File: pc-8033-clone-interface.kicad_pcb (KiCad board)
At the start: 2 copper layers, 95.2 x 67.3 mm, 19 parts, among them J2 80s31, U2 74LS32, U3 74LS04, U4 82C55A, U5 74LS30

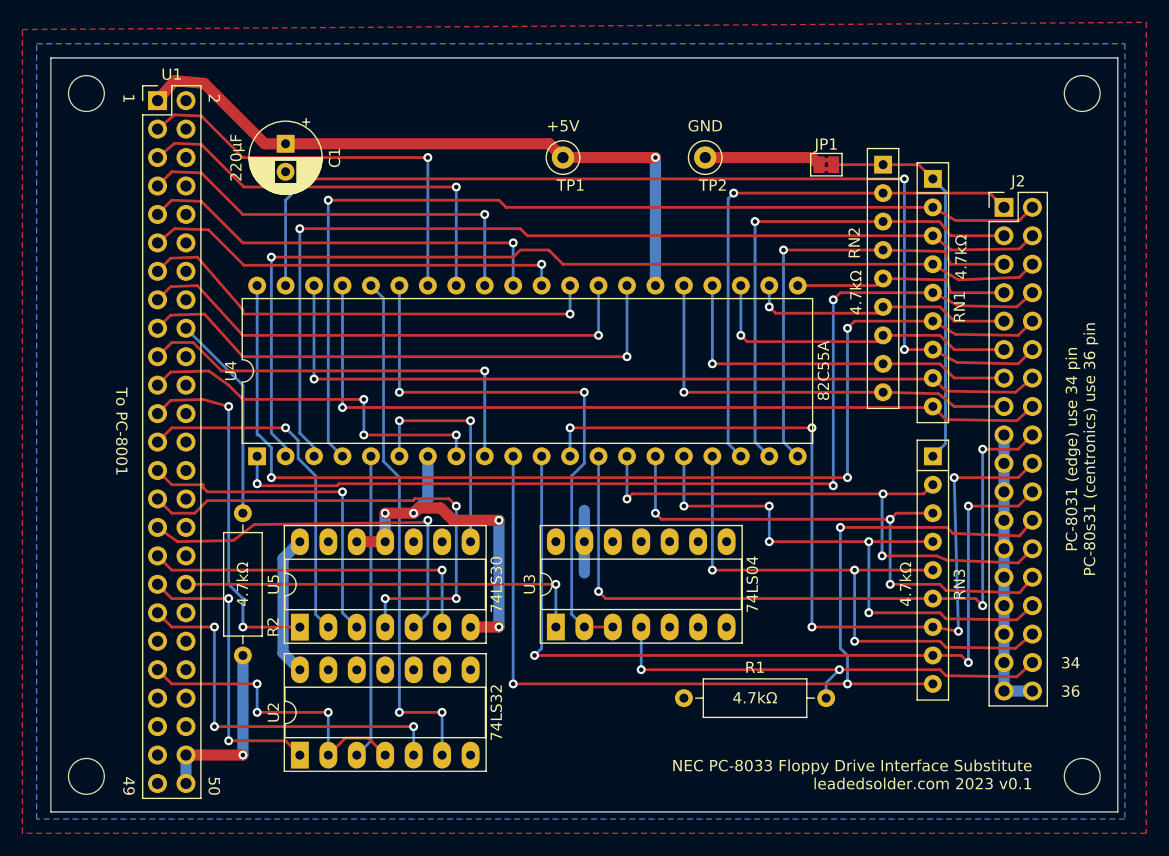
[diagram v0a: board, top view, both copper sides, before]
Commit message: Rotate 50-pin connector
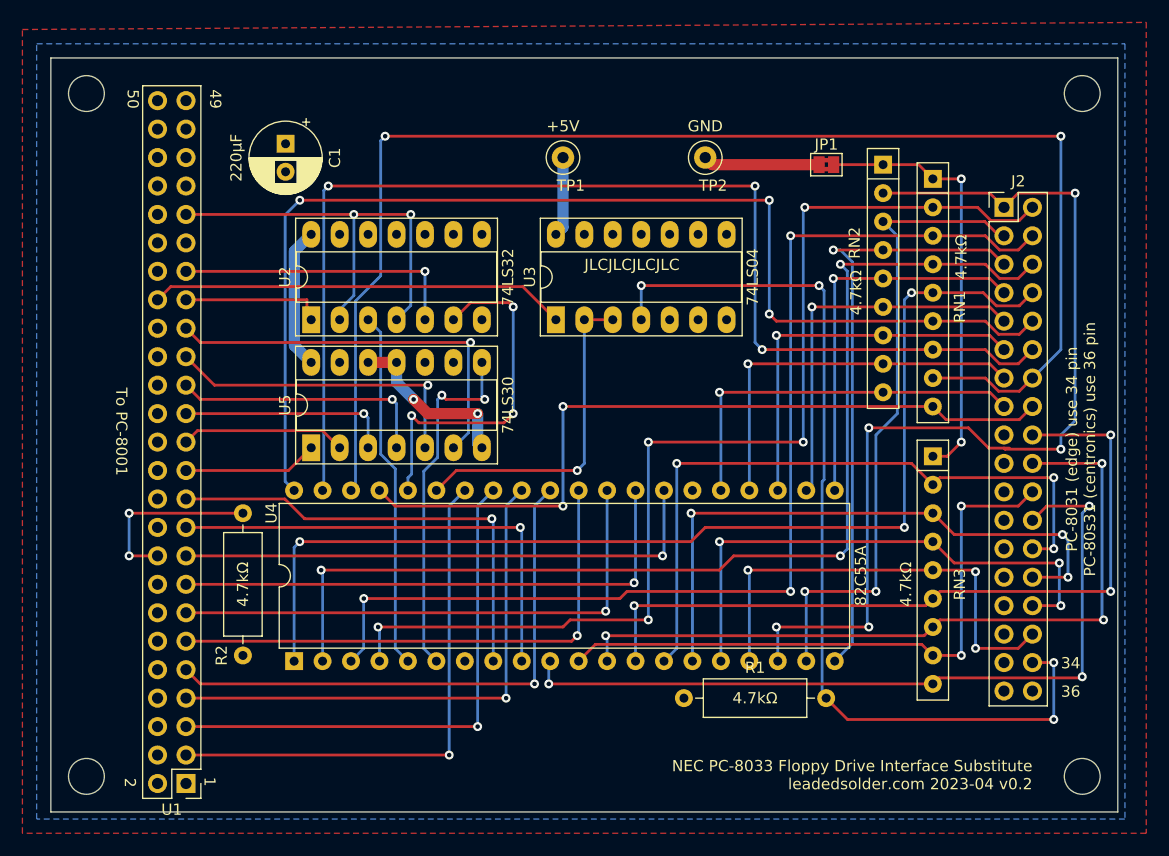
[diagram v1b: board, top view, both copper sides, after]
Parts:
- moved U1 61.0 mm to (116.8, 135.9), turned to 180 degrees
- moved U2 38.9 mm to (128.0, 94.5)
- moved U3 27.4 mm to (149.9, 94.5)
- moved U4 18.6 mm to (126.5, 125.0)
- moved U5 16.0 mm to (128.0, 105.9)
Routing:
- net GND: track 91.5 -> 26.3 mm, vias 5 -> 2
- net +5V: track 72.1 -> 19.8 mm, vias 1 -> 0
- net /pa6: track 73.5 -> 125.7 mm, vias 1 -> 2
- net Net-(J2-Pin_34): track 42.5 -> 84.3 mm, vias 2 -> 4
- net /pb0: track 48.8 -> 89.3 mm, vias 1 -> 5
- net /pc6: track 77.3 -> 55.4 mm, vias 3 -> 2
- net Net-(U1-AB5): track 45.2 -> 23.4 mm, vias 3 -> 1
- net /RESET: track 50.5 -> 29.6 mm, vias 2 -> 1
- net Net-(U1-AB2): track 32.2 -> 12.0 mm, vias 2 -> 0
- net /pc7: track 90.1 -> 71.1 mm
- net Net-(U1-AB3): track 31.3 -> 14.8 mm, vias 1 -> 0
- net /pb3: track 19.6 -> 34.7 mm, vias 0 -> 1
- net /pb2: track 39.3 -> 54.2 mm
- net /~{8255_WR}: track 46.8 -> 32.1 mm, vias 2 -> 3
- net /pa5: track 91.1 -> 105.5 mm
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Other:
- board text added: "JLCJLCJLCJLC"
- board text added: "NEC PC-8033 Floppy Drive Interface Substitute leadedsolder.com 2023-04 v0.2"
- board text removed: "NEC PC-8033 Floppy Drive Interface Substitute leadedsolder.com 2023 v0.1"

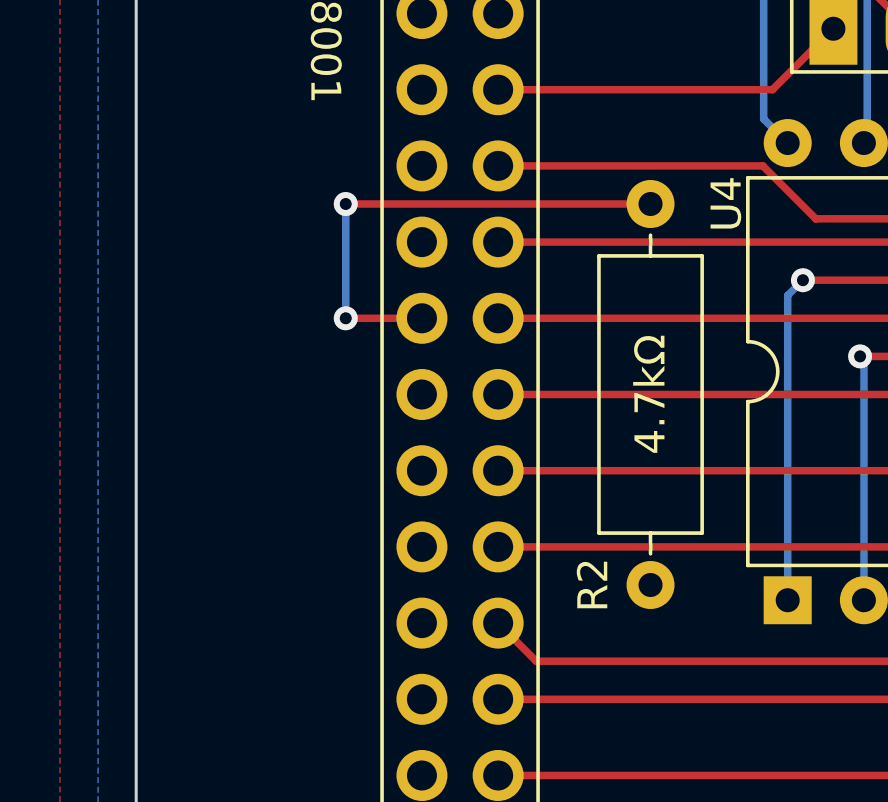
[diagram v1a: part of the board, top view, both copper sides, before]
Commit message: Short the EXTON pin instead of trying to gently pull it down
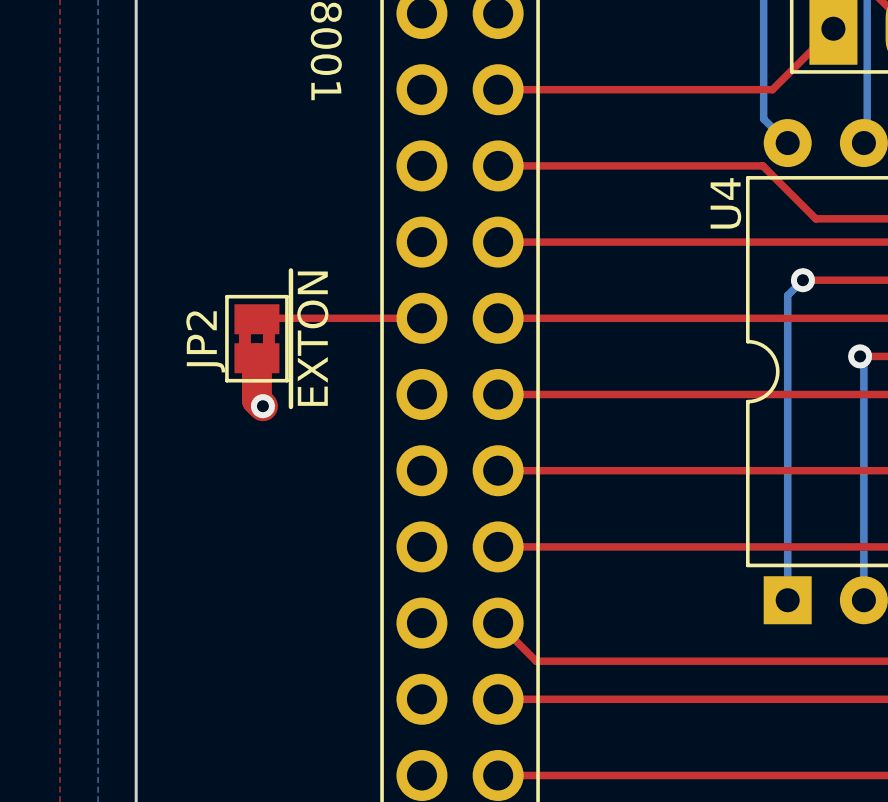
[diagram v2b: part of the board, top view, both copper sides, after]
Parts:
- removed R2: 4.7kΩ, Resistor_THT:R_Axial_DIN0309_L9.0mm_D3.2mm_P12.70mm_Horizontal
- added JP2: ~{EXTON}, Jumper:SolderJumper-2_P1.3mm_Bridged2Bar_Pad1.0x1.5mm, F.Cu at (108.8, 116.2)
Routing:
- net Net-(JP2-B): track 16.5 -> 5.51 mm, vias 2 -> 0
- net GND: track 26.3 -> 28.0 mm, vias 2 -> 3

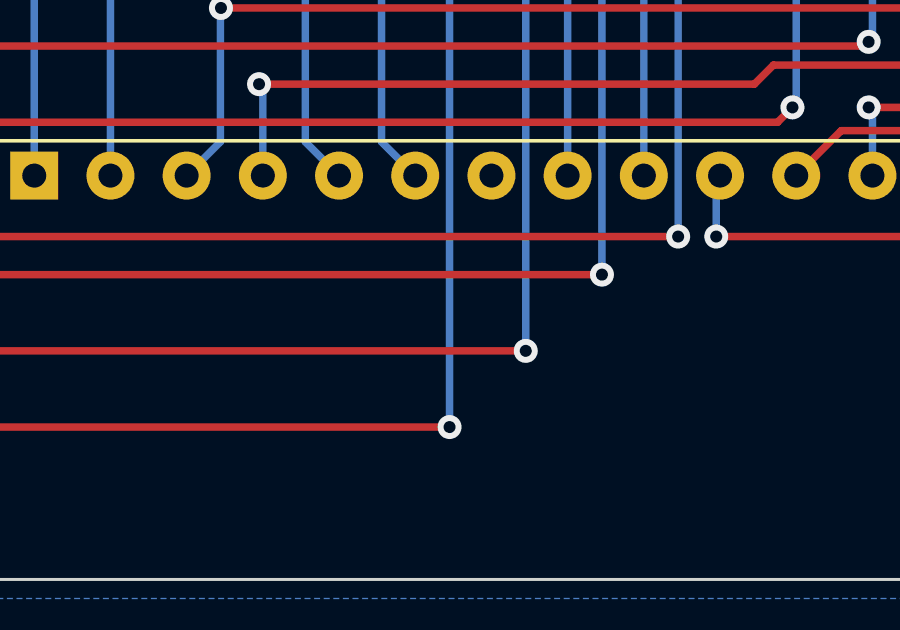
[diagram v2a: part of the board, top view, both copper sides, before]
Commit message: add a smaller decoupling cap on the 8255
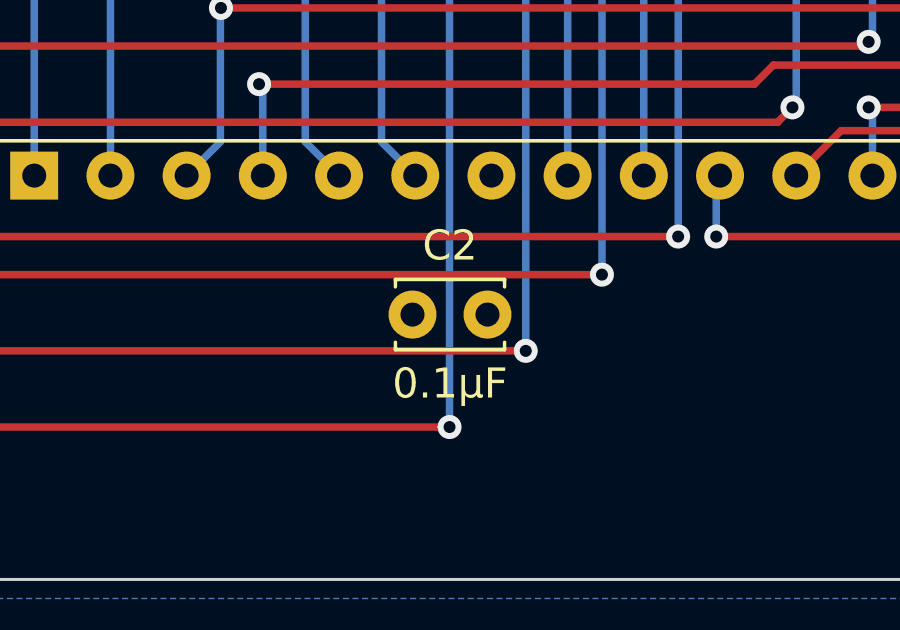
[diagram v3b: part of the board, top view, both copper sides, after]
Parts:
- added C2: 0.1µF, Capacitor_THT:C_Disc_D3.4mm_W2.1mm_P2.50mm, F.Cu at (139.1, 129.6)
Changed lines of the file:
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@@
   (net 84 "/~{8255_CS}")
   (net 85 "Net-(JP2-B)")
+  (footprint "Capacitor_THT:C_Disc_D3.4mm_W2.1mm_P2.50mm" (layer "F.Cu")
+    (at 139.1 129.6)
+    (descr "C, Disc series, Radial, pin pitch=2.50mm, , diameter*width=3.4*2.1mm^2, Capacitor, http://www.vishay.com/docs/45233/krseries.pdf")
+    (tags "C Disc series Radial pin pitch 2.50mm  diameter 3.4mm width 2.1mm Capacitor")
+    (property "Sheetfile" "pc-8033-clone-interface.kicad_sch")
+    (property "Sheetname" "")
+    (property "ki_description" "Unpolarized capacitor, small symbol")
+    (property "ki_keywords" "capacitor cap")
+    (attr through_hole)
+    (fp_text reference "C2" (at 1.25 -2.3) (layer "F.SilkS")
+        (effects (font (size 1 1) (thickness 0.15)))
+    )
+    (fp_text value "0.1µF" (at 1.25 2.3) (layer "F.SilkS")
+        (effects (font (size 1 1) (thickness 0.15)))
+    )
+    (fp_text user "${REFERENCE}" (at 1.25 0) (layer "F.Fab")
+        (effects (font (size 0.68 0.68) (thickness 0.102)))
+    )
+    (fp_line (start -0.57 -1.17) (end -0.57 -0.925)
+      (stroke (width 0.12) (type solid)) (layer "F.SilkS"))
+    (fp_line (start -0.57 -1.17) (end 3.07 -1.17)
+      (stroke (width 0.12) (type solid)) (layer "F.SilkS"))
+    (fp_line (start -0.57 0.925) (end -0.57 1.17)
+      (stroke (width 0.12) (type solid)) (layer "F.SilkS"))
+    (fp_line (start -0.57 1.17) (end 3.07 1.17)
+      (stroke (width 0.12) (type solid)) (layer "F.SilkS"))
+    (fp_line (start 3.07 -1.17) (end 3.07 -0.925)
+      (stroke (width 0.12) (type solid)) (layer "F.SilkS"))
+    (fp_line (start 3.07 0.925) (end 3.07 1.17)
+      (stroke (width 0.12) (type solid)) (layer "F.SilkS"))
+    (fp_line (start -1.05 -1.3) (end -1.05 1.3)
+      (stroke (width 0.05) (type solid)) (layer "F.CrtYd"))
+    (fp_line (start -1.05 1.3) (end 3.55 1.3)
+      (stroke (width 0.05) (type solid)) (layer "F.CrtYd"))
+    (fp_line (start 3.55 -1.3) (end -1.05 -1.3)
+      (stroke (width 0.05) (type solid)) (layer "F.CrtYd"))
+    (fp_line (start 3.55 1.3) (end 3.55 -1.3)
+      (stroke (width 0.05) (type solid)) (layer "F.CrtYd"))
+    (fp_line (start -0.45 -1.05) (end -0.45 1.05)
+      (stroke (width 0.1) (type solid)) (layer "F.Fab"))
+    (fp_line (start -0.45 1.05) (end 2.95 1.05)
+      (stroke (width 0.1) (type solid)) (layer "F.Fab"))
+    (fp_line (start 2.95 -1.05) (end -0.45 -1.05)
+      (stroke (width 0.1) (type solid)) (layer "F.Fab"))
+    (fp_line (start 2.95 1.05) (end 2.95 -1.05)
+      (stroke (width 0.1) (type solid)) (layer "F.Fab"))
+    (pad "1" thru_hole circle (at 0 0) (size 1.6 1.6) (drill 0.8) (layers "*.Cu" "*.Mask")
+      (net 1 "+5V") (pintype "passive"))
+    (pad "2" thru_hole circle (at 2.5 0) (size 1.6 1.6) (drill 0.8) (layers "*.Cu" "*.Mask")
+      (net 2 "GND") (pintype "passive"))
+    (model "${KICAD6_3DMODEL_DIR}/Capacitor_THT.3dshapes/C_Disc_D3.4mm_W2.1mm_P2.50mm.wrl"
+      (offset (xyz 0 0 0))
+      (scale (xyz 1 1 1))
+      (rotate (xyz 0 0 0))
+    )
+  )
   (footprint "Connector_PinHeader_2.54mm:PinHeader_2x18_P2.54mm_Vertical" (layer "F.Cu")
     (at 189.865 84.455)

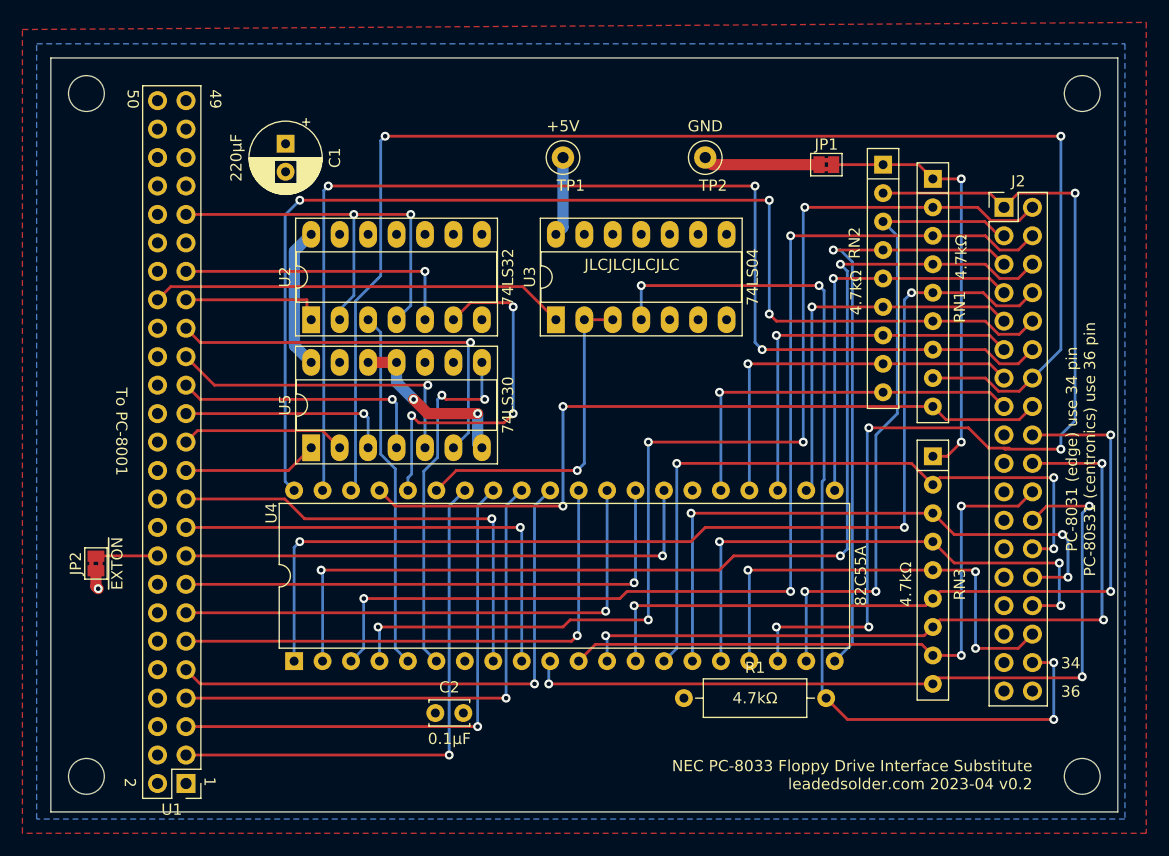
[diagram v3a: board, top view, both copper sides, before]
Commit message: Use weird Centronics pinout on board
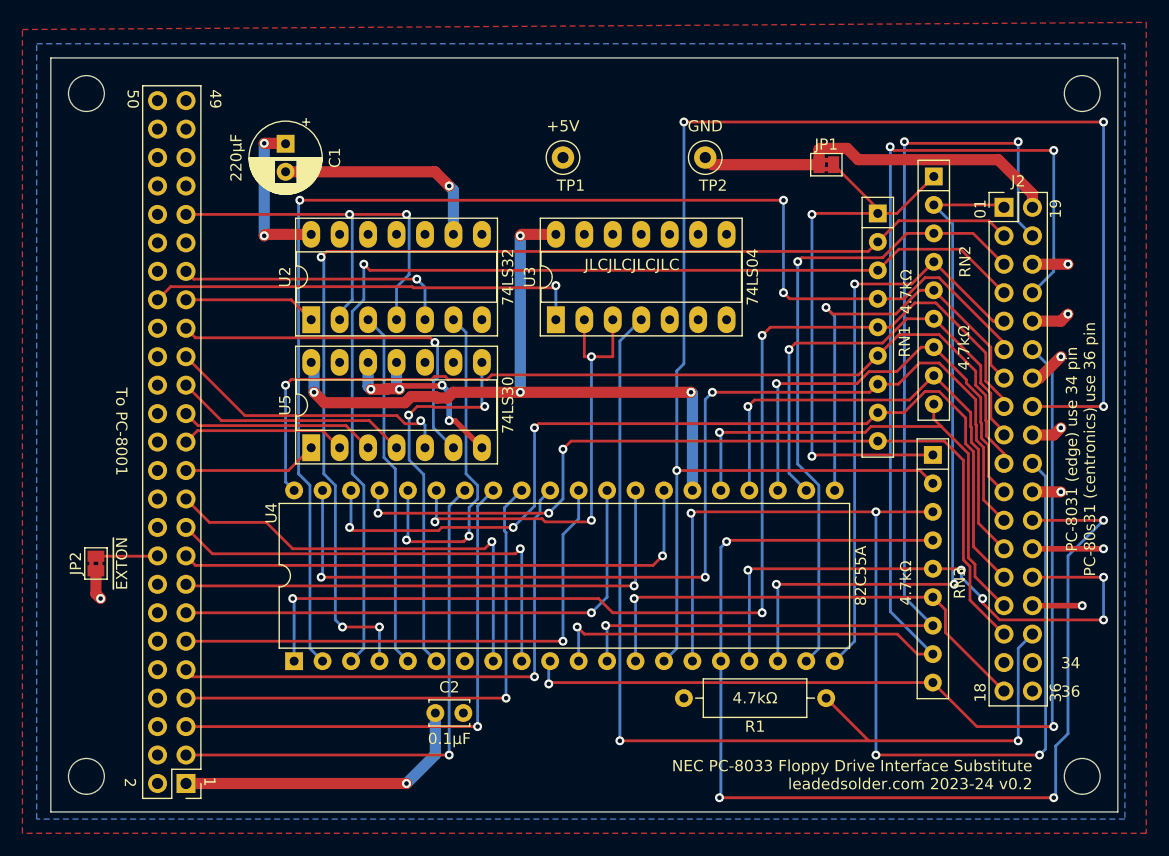
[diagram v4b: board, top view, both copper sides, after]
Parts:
- J2: footprint Connector_PinHeader_2.54mm:PinHeader_2x18_P2.54mm_Vertical -> PC-8001:Centronics_36_FDD
- moved RN1 5.80 mm to (178.6, 85.0)
- moved RN2 4.65 mm to (183.6, 81.7)
- moved RN3 0.12 mm to (183.5, 106.6)
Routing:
- net +5V: track 19.8 -> 104.8 mm, vias 0 -> 7
- net /pc0: track 61.1 -> 141.4 mm, vias 3 -> 4
- net GND: track 28.0 -> 101.0 mm, vias 3 -> 13
- net /pc2: track 48.3 -> 104.4 mm, vias 3 -> 4
- net /pc6: track 55.4 -> 110.9 mm, vias 2 -> 3
- net /pc1: track 54.4 -> 98.0 mm, vias 3 -> 4
- net /pa6: track 125.7 -> 84.3 mm, vias 2 -> 3
- net /pc5: track 67.6 -> 95.9 mm
- net /pc4: track 69.0 -> 43.4 mm, vias 3 -> 1
- net /pb0: track 89.3 -> 63.8 mm, vias 5 -> 2
- net /pa4: track 103.6 -> 84.1 mm, vias 3 -> 1
- net /pa2: track 99.8 -> 117.2 mm
- net Net-(JP1-B): track 38.5 -> 50.7 mm
- net /pc7: track 71.1 -> 83.3 mm, vias 3 -> 2
- net /pc3: track 41.0 -> 52.6 mm, vias 3 -> 5
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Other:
- board text added: "NEC PC-8033 Floppy Drive Interface Substitute leadedsolder.com 2023-24 v0.2"
- board text removed: "NEC PC-8033 Floppy Drive Interface Substitute leadedsolder.com 2023-04 v0.2"

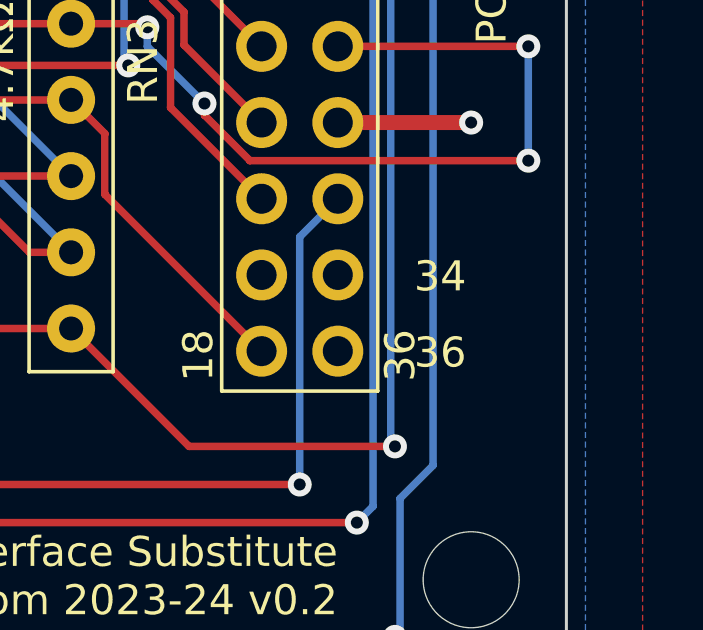
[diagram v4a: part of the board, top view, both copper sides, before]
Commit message: V2 sent to JLCPCB
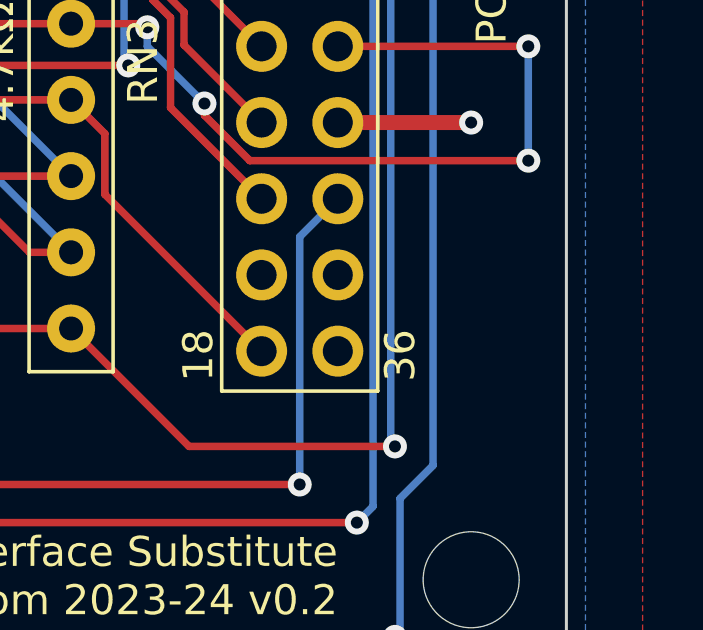
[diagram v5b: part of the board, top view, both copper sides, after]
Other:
- board text removed: "34"
- board text removed: "36"
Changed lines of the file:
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@@
       (drillshape 0)
       (scaleselection 1)
-      (outputdirectory "pc8033-clone-v1")
+      (outputdirectory "pc8033-clone-v2")
     )
   )
@@
   (gr_rect (start 104.775 71.12) (end 200.025 138.43)
     (stroke (width 0.1) (type default)) (fill none) (layer "Edge.Cuts"))
-  (gr_text "34" (at 194.945 125.73) (layer "F.SilkS")
-    (effects (font (size 1 1) (thickness 0.15)) (justify left bottom))
-  )
   (gr_text "1" (at 118.364 135.28881 -90) (layer "F.SilkS")
     (effects (font (size 1 1) (thickness 0.15)) (justify left bottom))
@@
     (effects (font (size 1 1) (thickness 0.15)) (justify right bottom))
   )
-  (gr_text "36" (at 194.945 128.27) (layer "F.SilkS")
-    (effects (font (size 1 1) (thickness 0.15)) (justify left bottom))
-  )
   (dimension (type aligned) (layer "Cmts.User")
